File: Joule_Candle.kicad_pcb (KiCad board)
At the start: 2 copper layers, 14 x 80 mm, 7 parts, among them Q1 BC817-40

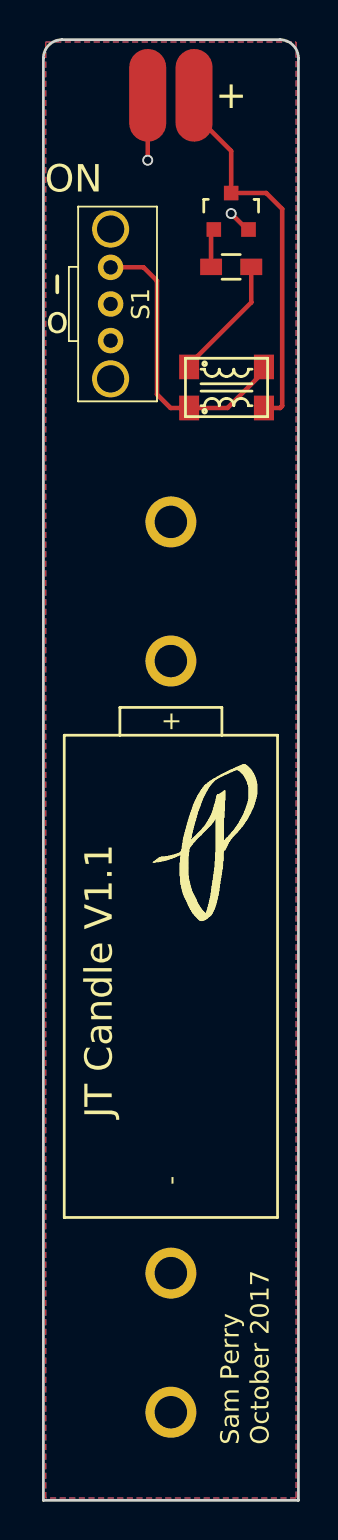
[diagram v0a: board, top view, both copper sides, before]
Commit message: update pcb with smd components
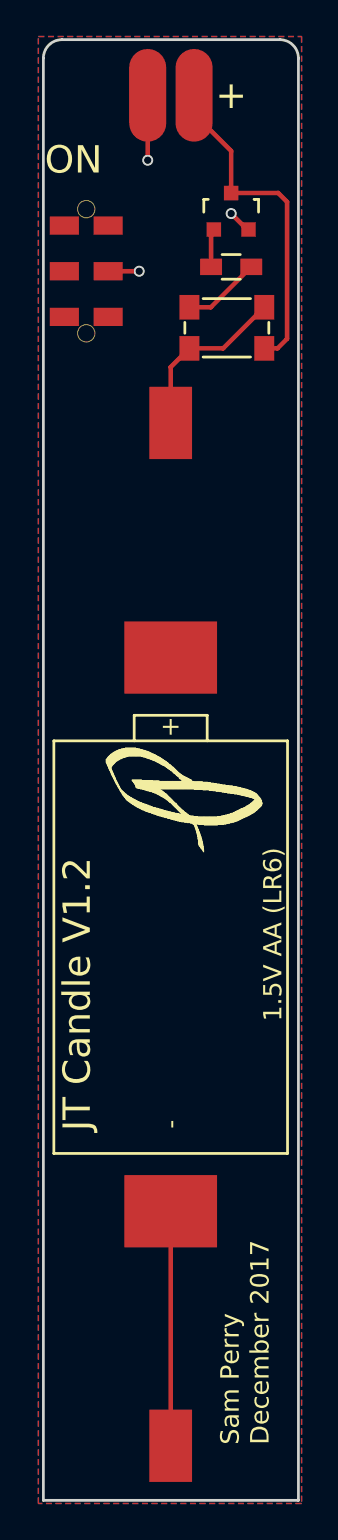
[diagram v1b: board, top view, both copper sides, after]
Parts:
- removed S1: SPDT, Switches:SPDT_OS102011MA1QN1
- added SW1: SW_DPDT_x2, lib_fp:DPDT_JS202011JAQN, F.Cu at (156.4, 64.5)
- 1.5V AA (LR6): renamed from BT1; footprint Battery:AA_PCB-Clip -> lib_fp:BK-53_MPD_AAClip
- Q1: value BC817-40 -> BC817-25
- R1: value 1K -> 6.8K
- moved 1.5V AA (LR6) 15.0 mm to (161.0, 100.8), turned to 0 degrees
- moved LOGO 5.68 mm to (157.4, 96.6), turned to 90 degrees
- moved L1 3.27 mm to (164.1, 67.6)
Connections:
- 1.5V AA (LR6) pad 2: GND -> Net-(BT1-Pad2)
- L1 pad 1: Net-(L1-Pad1) -> Net-(BT1-Pad1)
- L1 pad 3: Net-(L1-Pad1) -> Net-(BT1-Pad1)
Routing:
- net Net-(L1-Pad1): track 16.2 -> 0.00 mm
- net Net-(BT1-Pad2): track 0.00 -> 12.9 mm
- net Net-(BT1-Pad1): track 0.00 -> 9.54 mm
- net Net-(D1-Pad2): track 20.2 -> 17.4 mm
- net Net-(L1-Pad4): track 6.89 -> 4.30 mm
- net GND: track 3.85 -> 5.55 mm, vias 2 -> 3
- added copper zone on F.Cu, net Net-(BT1-Pad2)
- removed copper zone on F.Cu, net Net-(BT1-Pad1)
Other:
- board text added: "JT Candle V1.2"
- board text added: "Sam Perry December 2017"
- board text removed: "JT Candle V1.1"
- board text removed: "Sam Perry October 2017"
- board text removed: "o"
